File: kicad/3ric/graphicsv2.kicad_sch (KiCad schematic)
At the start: 39 parts

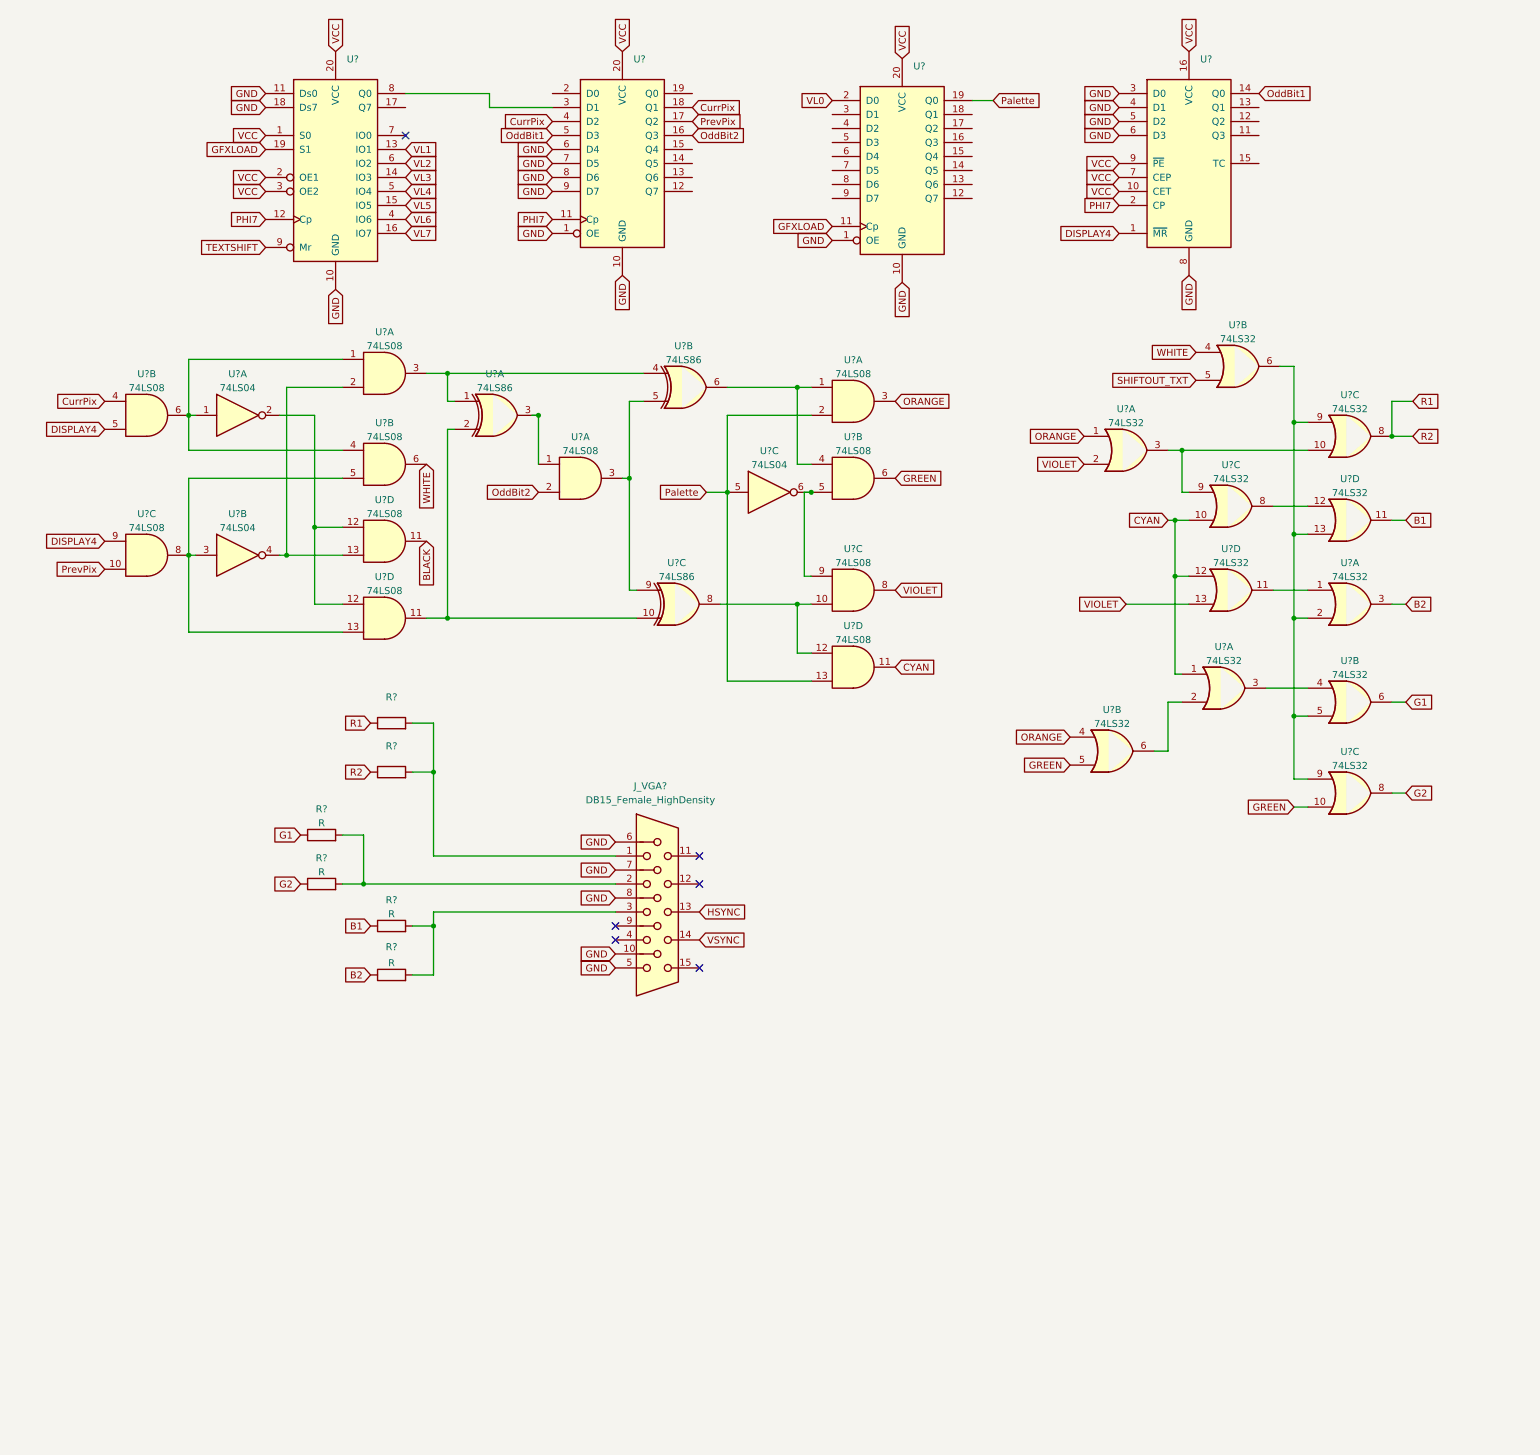
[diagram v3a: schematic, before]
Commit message: update schematic based on breadboard
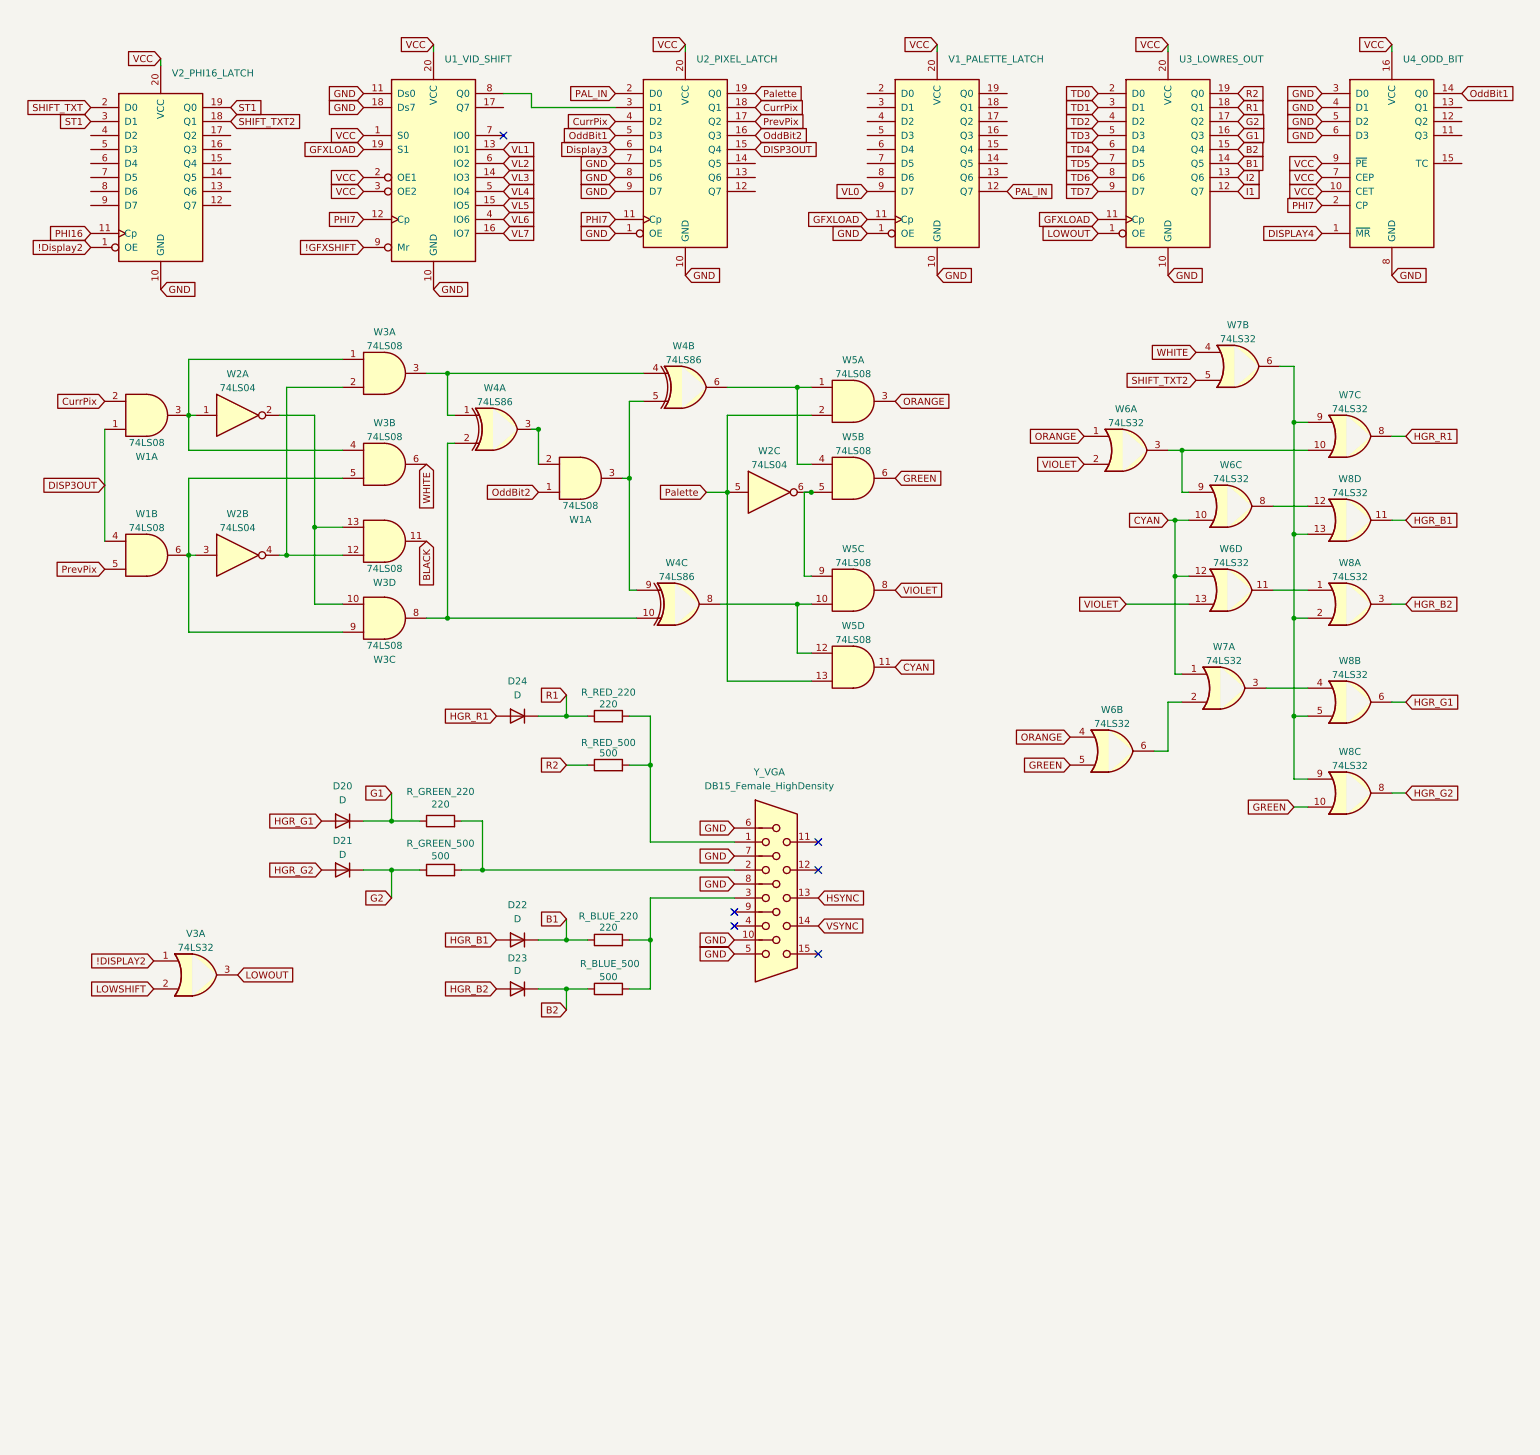
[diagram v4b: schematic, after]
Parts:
- added D20, D21, D22, D23, D24: D, symbol Device:D
- added U3_LOWRES_OUT, V2_PHI16_LATCH: ~, symbol 74xx:74LS574
- added V3: 74LS32, symbol 74xx:74LS32
- R_BLUE_220, R_GREEN_220: renamed from R?; value R -> 220
- R_BLUE_500, R_GREEN_500: renamed from R?; value R -> 500
- R_RED_220: renamed from R?; value ~ -> 220
- R_RED_500: renamed from R?; value ~ -> 500
- gave numbers to parts that had none: 13
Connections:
- net B1: now also D22.1 (K), U3_LOWRES_OUT.14 (Q5); no longer W8.11
- net B2: now also D23.1 (K), U3_LOWRES_OUT.15 (Q4); no longer W8.3
- net CurrPix: now also W1.2; no longer W1.4
- net DISPLAY4: no longer W1.5, W1.9
- net G1: now also D20.1 (K), U3_LOWRES_OUT.16 (Q3); no longer W8.6
- net G2: now also D21.1 (K), U3_LOWRES_OUT.17 (Q2); no longer W8.8
- net GFXLOAD: now also U3_LOWRES_OUT.11 (Cp)
- net GND: now also U3_LOWRES_OUT.10 (GND), V2_PHI16_LATCH.10 (GND); no longer U2_PIXEL_LATCH.6 (D4)
- net OddBit2: now also W1.1; no longer W1.2
- net Palette: now also U2_PIXEL_LATCH.19 (Q0); no longer V1_PALETTE_LATCH.19 (Q0)
- net PrevPix: now also W1.5; no longer W1.10
- net R1: now also D24.1 (K), U3_LOWRES_OUT.18 (Q1); no longer R_RED_500.1, W7.8
- net VCC: now also U3_LOWRES_OUT.20 (VCC), V2_PHI16_LATCH.20 (VCC)
- net VL0: now also V1_PALETTE_LATCH.9 (D7); no longer V1_PALETTE_LATCH.2 (D0)
- net at W4.10, W4.2: now also W3.8; no longer W3.11
- net at W4.3: now also W1.2; no longer W1.1
- net at W2.3, W3.5: now also W1.6, W3.9; no longer W1.8, W3.13
- net at W2.4, W3.2: now also W3.12; no longer W3.13
- net at W2.1, W3.1, W3.4: now also W1.3; no longer W1.6
- net PAL_IN: now reaches V1_PALETTE_LATCH.12 (Q7)
- net PAL_IN: now also U2_PIXEL_LATCH.2 (D0)
- net DISP3OUT: now reaches U2_PIXEL_LATCH.15 (Q4)
- net DISP3OUT: now also W1.1, W1.4
- net SHIFTOUT_TXT renamed SHIFT_TXT2
- net SHIFT_TXT2: now also V2_PHI16_LATCH.18 (Q1)
- net TEXTSHIFT renamed !GFXSHIFT
- new net: W2.2, W3.10, W3.13
- new net !DISPLAY2: V3.1
- new net !Display2: V2_PHI16_LATCH.1 (OE)
- new net Display3: U2_PIXEL_LATCH.6 (D4)
- new net HGR_B1: D22.2 (A), W8.11
- new net HGR_B2: D23.2 (A), W8.3
- new net HGR_G1: D20.2 (A), W8.6
- new net HGR_G2: D21.2 (A), W8.8
- new net HGR_R1: D24.2 (A), W7.8
- new net I1: U3_LOWRES_OUT.12 (Q7)
- new net I2: U3_LOWRES_OUT.13 (Q6)
- new net LOWOUT: U3_LOWRES_OUT.1 (OE), V3.3
- new net LOWSHIFT: V3.2
- new net PHI16: V2_PHI16_LATCH.11 (Cp)
- new net R2: R_RED_500.1, U3_LOWRES_OUT.19 (Q0)
- new net SHIFT_TXT: V2_PHI16_LATCH.2 (D0)
- new net ST1: V2_PHI16_LATCH.19 (Q0), V2_PHI16_LATCH.3 (D1)
- new net TD0: U3_LOWRES_OUT.2 (D0)
- new net TD1: U3_LOWRES_OUT.3 (D1)
- new net TD2: U3_LOWRES_OUT.4 (D2)
- new net TD3: U3_LOWRES_OUT.5 (D3)
- new net TD4: U3_LOWRES_OUT.6 (D4)
- new net TD5: U3_LOWRES_OUT.7 (D5)
- new net TD6: U3_LOWRES_OUT.8 (D6)
- new net TD7: U3_LOWRES_OUT.9 (D7)
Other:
- moved on the sheet: R_BLUE_220, R_BLUE_500, R_GREEN_220, R_GREEN_500, R_RED_220, R_RED_500, U1_VID_SHIFT, U2_PIXEL_LATCH, U4_ODD_BIT, V1_PALETTE_LATCH, W4A, Y_VGA

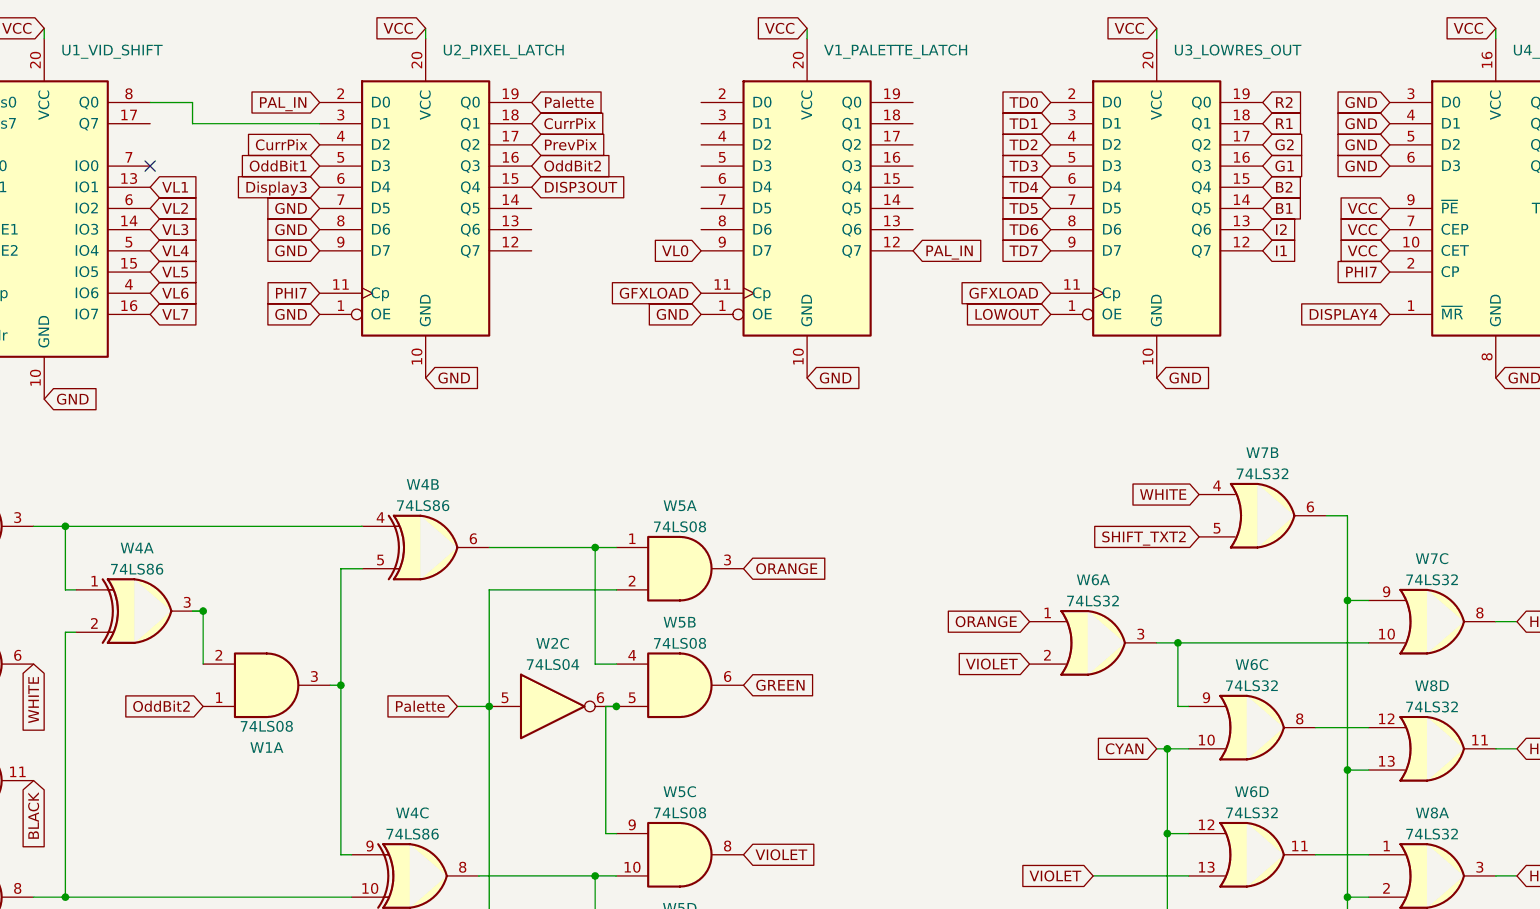
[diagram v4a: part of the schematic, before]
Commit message: add a pdf of the breadboard layout
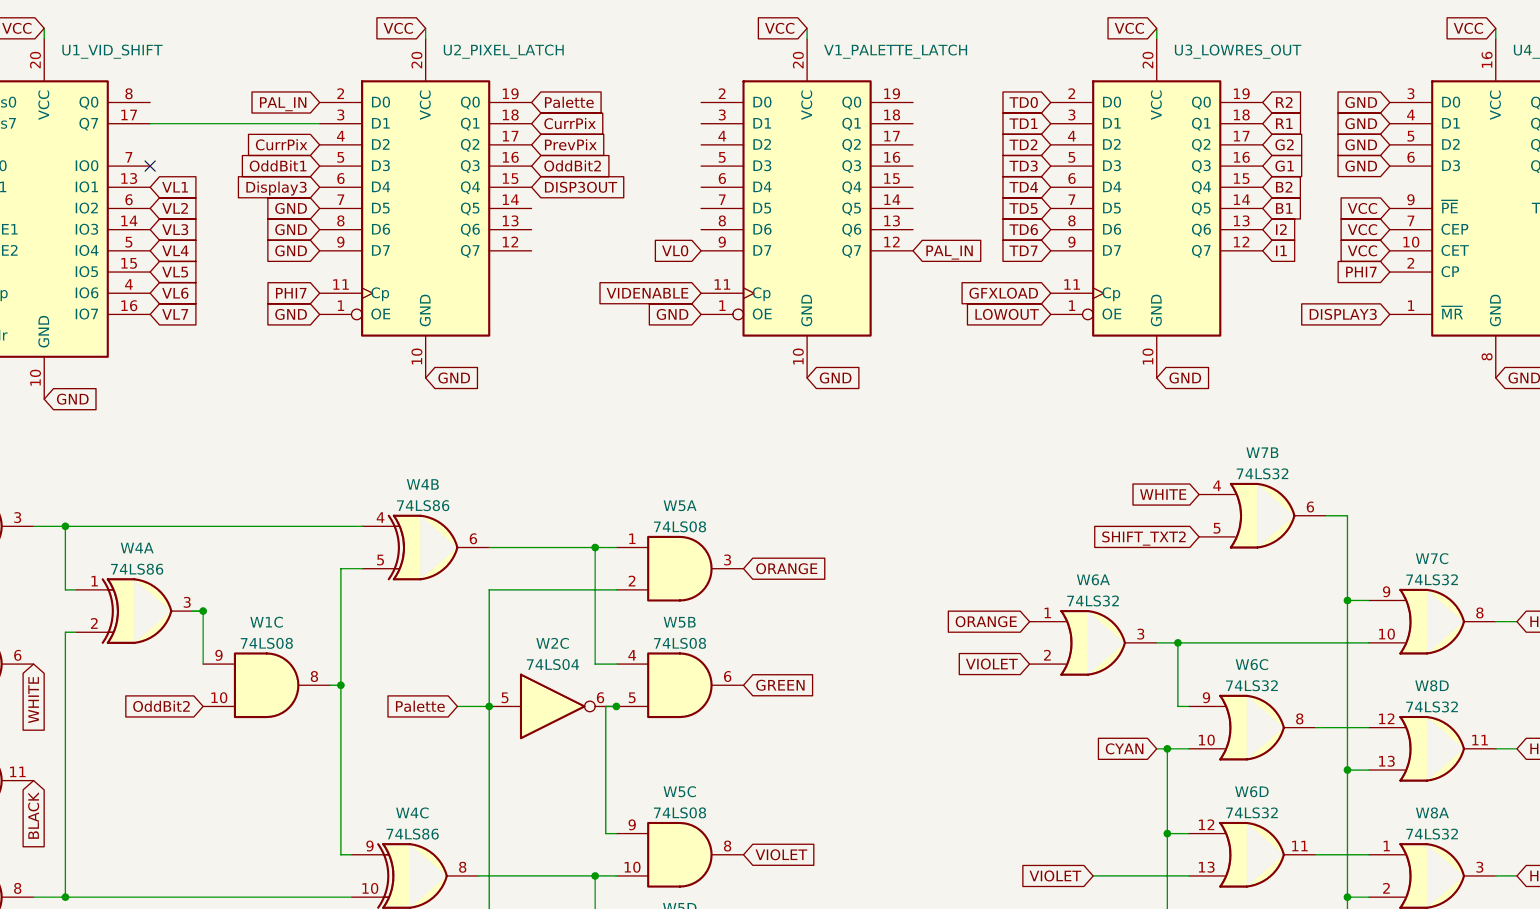
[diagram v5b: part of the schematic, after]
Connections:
- net GFXLOAD: no longer V1_PALETTE_LATCH.11 (Cp)
- net OddBit2: now also W1.10; no longer W1.1
- net at W4.3: now also W1.9; no longer W1.2
- net at W4.5, W4.9: now also W1.8; no longer W1.3
- net at U1_VID_SHIFT.17 (Q7): now also U2_PIXEL_LATCH.3 (D1)
- net at U1_VID_SHIFT.8 (Q0): no longer U2_PIXEL_LATCH.3 (D1)
- net DISPLAY4 renamed DISPLAY3
- new net VIDENABLE: V1_PALETTE_LATCH.11 (Cp)
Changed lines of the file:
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@@
 	(wire
 		(pts
+			(xy 100.33 29.21) (xy 120.65 29.21)
+		)
+		(stroke
+			(width 0)
+			(type default)
+		)
+	)
+	(wire
+		(pts
 			(xy 90.17 77.47) (xy 125.73 77.47)
 		)
@@
 	(wire
 		(pts
-			(xy 105.41 26.67) (xy 105.41 29.21)
-		)
-		(stroke
-			(width 0)
-			(type default)
-		)
-	)
-	(wire
-		(pts
 			(xy 238.76 134.62) (xy 246.38 134.62)
 		)
@@
 	(wire
 		(pts
-			(xy 100.33 26.67) (xy 105.41 26.67)
-		)
-		(stroke
-			(width 0)
-			(type default)
-		)
-	)
-	(wire
-		(pts
 			(xy 264.16 153.67) (xy 261.62 153.67)
 		)
@@
 	(wire
 		(pts
-			(xy 105.41 29.21) (xy 120.65 29.21)
-		)
-		(stroke
-			(width 0)
-			(type default)
-		)
-	)
-	(wire
-		(pts
 			(xy 140.97 85.09) (xy 140.97 99.06)
 		)
@@
 		)
 	)
-	(global_label "DISPLAY4"
+	(global_label "DISPLAY3"
 		(shape input)
 		(at 248.92 52.07 180)
@@
 		)
 		(property "Intersheetrefs" "${INTERSHEET_REFS}"
-			(at 237.7379 51.9906 0)
+			(at 237.1657 52.07 0)
 			(effects
 				(font
@@
 		)
 	)
-	(global_label "GFXLOAD"
+	(global_label "VIDENABLE"
 		(shape input)
 		(at 166.37 49.53 180)
@@
 		)
 		(property "Intersheetrefs" "${INTERSHEET_REFS}"
-			(at 155.6717 49.4506 0)
+			(at 153.4062 49.53 0)
 			(effects
 				(font
@@
 		(lib_id "74xx:74LS08")
 		(at 114.3 96.52 0)
-		(mirror x)
-		(unit 1)
+		(unit 3)
 		(exclude_from_sim no)
 		(in_bom yes)
@@
 		(dnp no)
 		(property "Reference" "W1"
-			(at 114.3 104.0298 0)
+			(at 114.3 89.0102 0)
 			(effects
 				(font
@@
 		)
 		(property "Value" "74LS08"
-			(at 114.3 101.4929 0)
+			(at 114.3 91.5471 0)
 			(effects
 				(font
@@
 				(path "/e63e39d7-6ac0-4ffd-8aa3-1841a4541b55/896392e0-4074-452d-a014-a15ee50eb391"
 					(reference "W1")
-					(unit 1)
+					(unit 3)
 				)
 			)
